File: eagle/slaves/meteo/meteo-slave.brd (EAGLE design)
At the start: 49.5 x 49.5 mm, 37 parts, among them CON1 SPI, IC1 MCP1703CB, J2 RJ12RIGHTANGLE-I2C, J3 RJ12RIGHTANGLE-I2C, U1 ATMEGA328P_TQFP, X1 8MHz, X2 1503_09, X3 1503_09

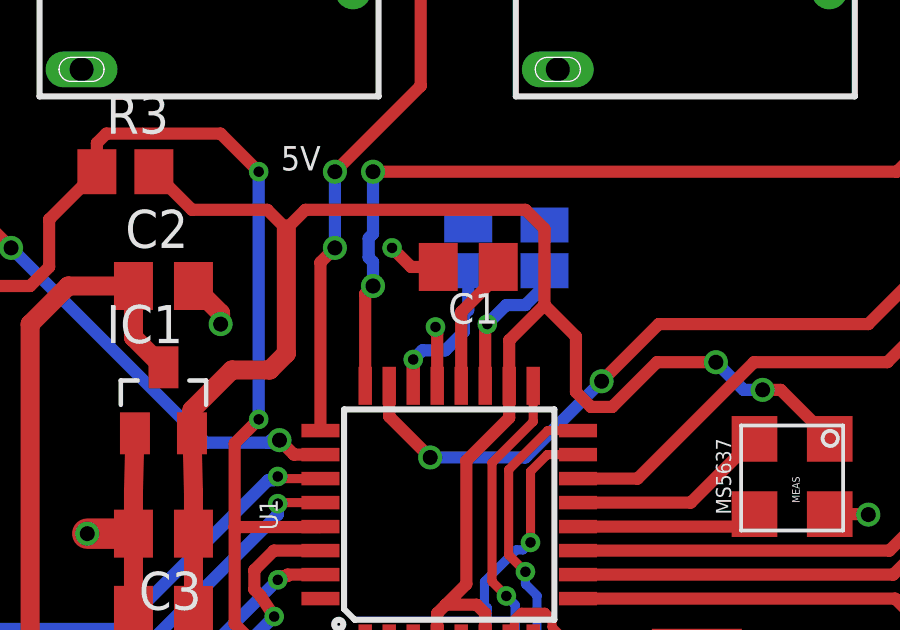
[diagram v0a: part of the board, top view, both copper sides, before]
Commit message: remove meteo capacitor for AREF
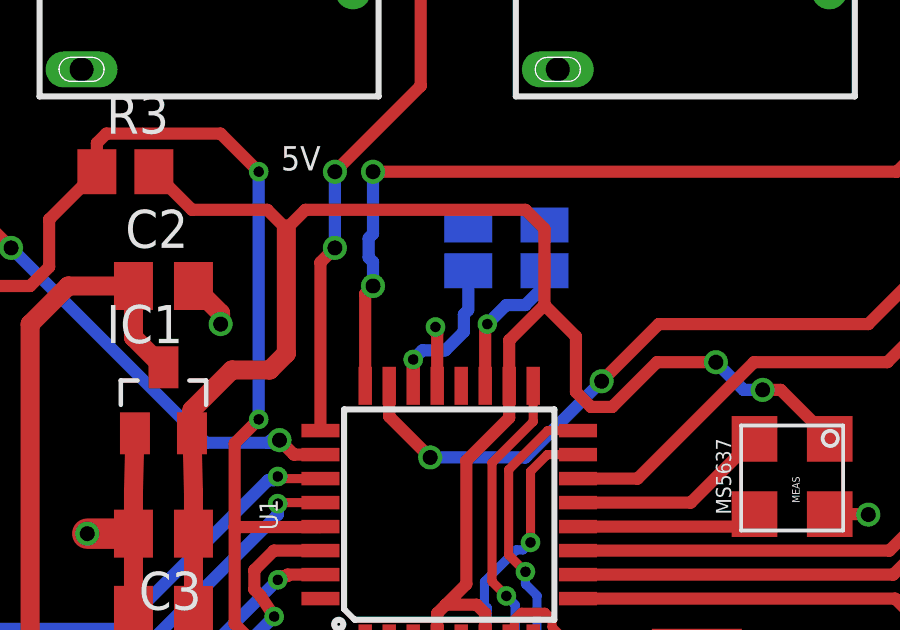
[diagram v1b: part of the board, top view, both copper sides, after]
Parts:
- removed C1: 100nF, rcl:C0805K
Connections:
- removed net AREF: C1.1, U1.20
- net GND: no longer C1.2
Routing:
- net AREF: track 4.47 -> 0.00 mm
- net GND: track 34.3 -> 32.5 mm, vias 13 -> 12
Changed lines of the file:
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@@
 <attribute name="VALUE" x="26.019" y="6.70695" size="1.016" layer="27" rot="R180"/>
-</element>
-<element name="C1" library="rcl" library_urn="urn:adsk.eagle:library:334" package="C0805K" package3d_urn="urn:adsk.eagle:package:23681/2" value="100nF" x="29.21" y="28.575" smashed="yes" rot="R180">
-<attribute name="ELECROW" value="C49678" x="29.21" y="28.575" size="1.778" layer="27" rot="R180" display="off"/>
-<attribute name="LCSC" value="C49678" x="29.21" y="28.575" size="1.778" layer="27" rot="R180" display="off"/>
-<attribute name="MPN" value="80-C1206C104K5R" x="29.21" y="28.575" size="1.778" layer="27" rot="R180" display="off"/>
-<attribute name="NAME" x="30.21" y="27.7" size="1.016" layer="25" rot="R180"/>
-<attribute name="VALUE" x="31.06725" y="30.8179" size="1.016" layer="27" rot="R180"/>
 </element>
 <element name="C5" library="rcl" library_urn="urn:adsk.eagle:library:334" package="C0805K" package3d_urn="urn:adsk.eagle:package:23681/2" value="100nF" x="27.305" y="12.7" smashed="yes" rot="R180">
@@
 <contactref element="C8" pad="1"/>
 <contactref element="C7" pad="1"/>
-<contactref element="C1" pad="2"/>
 <wire x1="40.005" y1="11.795" x2="40.005" y2="13.605" width="0.3048" layer="1"/>
 <wire x1="40.005" y1="11.795" x2="40.91" y2="11.795" width="0.3048" layer="1"/>
@@
 <wire x1="40.97168125" y1="14.5526" x2="41.16968125" y2="14.7506" width="0.3048" layer="1"/>
 <wire x1="41.16968125" y1="14.7506" x2="41.3824" y2="14.7506" width="0.3048" layer="1"/>
-<wire x1="28.21" y1="28.575" x2="27.305" y2="28.575" width="0.4064" layer="1"/>
-<wire x1="27.305" y1="28.575" x2="26.67" y2="29.21" width="0.4064" layer="1"/>
-<via x="26.67" y="29.21" extent="1-16" drill="0.35"/>
 <contactref element="U$1" pad="GND"/>
 <contactref element="U2" pad="GND"/>
@@
 <wire x1="2.286" y1="37.719" x2="2.54" y2="37.465" width="0.4064" layer="1"/>
 <via x="2.54" y="37.465" extent="1-16" drill="0.5"/>
+<wire x1="41.245" y1="38.36" x2="45.72" y2="40.005" width="0" layer="19" extent="1-1"/>
+<wire x1="31.75" y1="29.972" x2="41.245" y2="38.36" width="0" layer="19" extent="16-16"/>
+<wire x1="29.21" y1="29.972" x2="31.75" y2="29.972" width="0" layer="19" extent="16-16"/>
+<wire x1="28.1178" y1="26.57475" x2="29.21" y2="29.972" width="0" layer="19" extent="16-16"/>
+<wire x1="20.955" y1="26.67" x2="28.1178" y2="26.57475" width="0" layer="19" extent="1-1"/>
+<wire x1="18.1" y1="23.03" x2="20.955" y2="26.67" width="0" layer="19" extent="1-1"/>
+<wire x1="28.975" y1="16.0274" x2="28.175" y2="24.6126" width="0" layer="19" extent="1-1"/>
+<wire x1="27.375" y1="16.0274" x2="28.975" y2="16.0274" width="0" layer="19" extent="1-1"/>
+<wire x1="28.575" y1="8.1188" x2="25.4" y2="10.795" width="0" layer="19" extent="1-1"/>
+<wire x1="24.13" y1="4.445" x2="28.575" y2="8.1188" width="0" layer="19" extent="1-1"/>
+<wire x1="21.59" y1="4.445" x2="24.13" y2="4.445" width="0" layer="19" extent="1-1"/>
+<wire x1="38.1" y1="4.445" x2="30.48" y2="6.985" width="0" layer="19" extent="1-1"/>
+<wire x1="41.275" y1="11.43" x2="39.69" y2="4.445" width="0" layer="19" extent="1-1"/>
+<wire x1="45.72" y1="16.51" x2="41.3824" y2="14.7506" width="0" layer="19" extent="1-1"/>
+<wire x1="42.545" y1="20.32" x2="45.72" y2="16.51" width="0" layer="19" extent="1-1"/>
+<wire x1="25.37" y1="38.36" x2="29.21" y2="29.972" width="0" layer="19" extent="16-16"/>
+<wire x1="6.745" y1="16.51" x2="16.51" y2="19.685" width="0" layer="19" extent="1-1"/>
+<wire x1="6.745" y1="14.47" x2="6.745" y2="16.51" width="0" layer="19" extent="1-1"/>
+<wire x1="6.745" y1="30.345" x2="18.1" y2="23.03" width="0" layer="19" extent="1-1"/>
+<wire x1="6.745" y1="32.385" x2="6.745" y2="30.345" width="0" layer="19" extent="1-1"/>
+<wire x1="7.62" y1="37.465" x2="6.745" y2="32.385" width="0" layer="19" extent="1-1"/>
+<wire x1="2.54" y1="37.465" x2="7.62" y2="37.465" width="0" layer="19" extent="1-1"/>
 </signal>
 <signal name="SCK">
@@
 <signal name="N$16">
 </signal>
-<signal name="AREF">
-<contactref element="C1" pad="1"/>
-<wire x1="30.21" y1="28.305" x2="30.21" y2="28.575" width="0.4064" layer="1"/>
-<wire x1="28.975" y1="27.07" x2="30.21" y2="28.305" width="0.4064" layer="1"/>
-<contactref element="U1" pad="20"/>
-<wire x1="28.975" y1="24.6126" x2="28.975" y2="27.07" width="0.4064" layer="1"/>
-</signal>
 <signal name="TX">

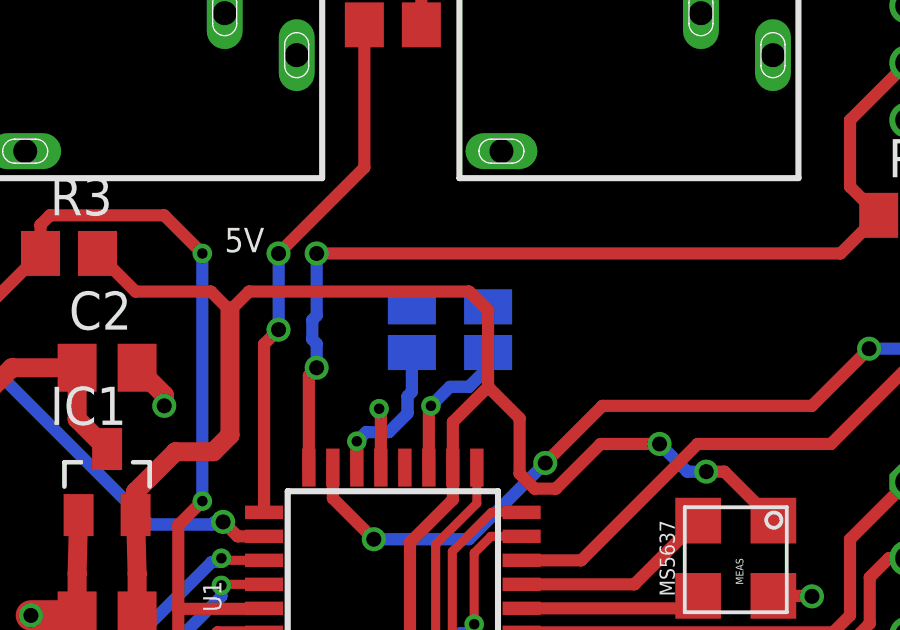
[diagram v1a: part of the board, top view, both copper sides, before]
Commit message: move address selector pad in meteo board
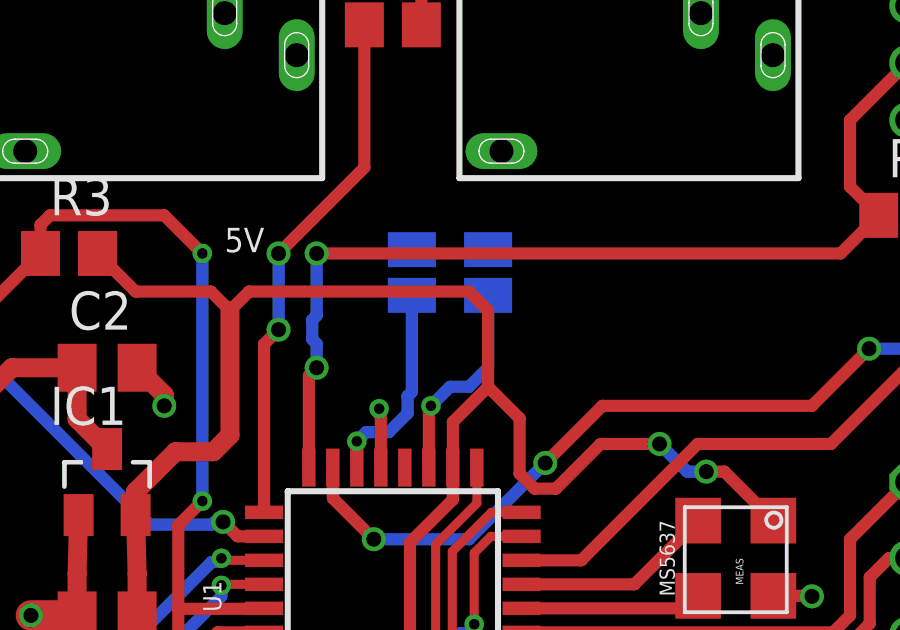
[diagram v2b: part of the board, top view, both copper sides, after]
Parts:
- moved SJ1 1.90 mm to (31.8, 31.1)
- moved SJ2 1.90 mm to (29.2, 31.1)
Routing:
- net A7: track 5.04 -> 6.95 mm
- net A6: track 5.03 -> 6.93 mm
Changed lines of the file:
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@@
 <layer number="199" name="Contour" color="7" fill="1" visible="no" active="yes"/>
 <layer number="200" name="200bmp" color="63" fill="10" visible="no" active="yes"/>
-<layer number="201" name="201bmp" color="63" fill="10" visible="yes" active="yes"/>
+<layer number="201" name="201bmp" color="63" fill="10" visible="no" active="yes"/>
 <layer number="202" name="202bmp" color="15" fill="1" visible="no" active="yes"/>
 <layer number="203" name="203bmp" color="2" fill="10" visible="no" active="yes"/>
@@
 <attribute name="VALUE" x="13.74645" y="14.65725" size="1.016" layer="27" rot="R270"/>
 </element>
-<element name="SJ1" library="jumper" library_urn="urn:adsk.eagle:library:252" package="SJ" package3d_urn="urn:adsk.eagle:package:15471/1" value="A0" x="31.75" y="29.21" smashed="yes" rot="MR90">
-<attribute name="NAME" x="32.893" y="27.559" size="1.27" layer="26" ratio="10" rot="MR90"/>
-<attribute name="VALUE" x="31.75" y="29.6101" size="0.02" layer="28" rot="MR90"/>
+<element name="SJ1" library="jumper" library_urn="urn:adsk.eagle:library:252" package="SJ" package3d_urn="urn:adsk.eagle:package:15471/1" value="A0" x="31.75" y="31.115" smashed="yes" rot="MR90">
+<attribute name="NAME" x="32.893" y="29.464" size="1.27" layer="26" ratio="10" rot="MR90"/>
+<attribute name="VALUE" x="31.75" y="31.5151" size="0.02" layer="28" rot="MR90"/>
 </element>
-<element name="SJ2" library="jumper" library_urn="urn:adsk.eagle:library:252" package="SJ" package3d_urn="urn:adsk.eagle:package:15471/1" value="A1" x="29.21" y="29.21" smashed="yes" rot="MR90">
-<attribute name="NAME" x="30.353" y="27.559" size="1.27" layer="26" ratio="10" rot="MR90"/>
-<attribute name="VALUE" x="29.21" y="29.6101" size="0.02" layer="28" rot="MR90"/>
+<element name="SJ2" library="jumper" library_urn="urn:adsk.eagle:library:252" package="SJ" package3d_urn="urn:adsk.eagle:package:15471/1" value="A1" x="29.21" y="31.115" smashed="yes" rot="MR90">
+<attribute name="NAME" x="30.353" y="29.464" size="1.27" layer="26" ratio="10" rot="MR90"/>
+<attribute name="VALUE" x="29.21" y="31.5151" size="0.02" layer="28" rot="MR90"/>
 </element>
 <element name="C7" library="rcl" library_urn="urn:adsk.eagle:library:334" package="C0805K" package3d_urn="urn:adsk.eagle:package:23681/2" value="18pF" x="40.005" y="10.795" smashed="yes" rot="R270">
@@
 <via x="2.54" y="37.465" extent="1-16" drill="0.5"/>
 <wire x1="41.245" y1="38.36" x2="45.72" y2="40.005" width="0" layer="19" extent="1-1"/>
-<wire x1="31.75" y1="29.972" x2="41.245" y2="38.36" width="0" layer="19" extent="16-16"/>
-<wire x1="29.21" y1="29.972" x2="31.75" y2="29.972" width="0" layer="19" extent="16-16"/>
-<wire x1="28.1178" y1="26.57475" x2="29.21" y2="29.972" width="0" layer="19" extent="16-16"/>
+<wire x1="31.75" y1="31.877" x2="41.245" y2="38.36" width="0" layer="19" extent="16-16"/>
+<wire x1="29.21" y1="31.877" x2="31.75" y2="31.877" width="0" layer="19" extent="16-16"/>
+<wire x1="28.1178" y1="26.57475" x2="29.21" y2="31.877" width="0" layer="19" extent="16-16"/>
 <wire x1="20.955" y1="26.67" x2="28.1178" y2="26.57475" width="0" layer="19" extent="1-1"/>
 <wire x1="18.1" y1="23.03" x2="20.955" y2="26.67" width="0" layer="19" extent="1-1"/>
@@
 <wire x1="45.72" y1="16.51" x2="41.3824" y2="14.7506" width="0" layer="19" extent="1-1"/>
 <wire x1="42.545" y1="20.32" x2="45.72" y2="16.51" width="0" layer="19" extent="1-1"/>
-<wire x1="25.37" y1="38.36" x2="29.21" y2="29.972" width="0" layer="19" extent="16-16"/>
+<wire x1="25.37" y1="38.36" x2="29.21" y2="31.877" width="0" layer="19" extent="16-16"/>
 <wire x1="6.745" y1="16.51" x2="16.51" y2="19.685" width="0" layer="19" extent="1-1"/>
 <wire x1="6.745" y1="14.47" x2="6.745" y2="16.51" width="0" layer="19" extent="1-1"/>
@@
 <wire x1="30.48" y1="27.305" x2="31.115" y2="27.305" width="0.4064" layer="16"/>
 <wire x1="31.115" y1="27.305" x2="31.75" y2="27.94" width="0.4064" layer="16"/>
-<wire x1="31.75" y1="27.94" x2="31.75" y2="28.448" width="0.4064" layer="16"/>
+<wire x1="31.75" y1="27.94" x2="31.75" y2="30.353" width="0.4064" layer="16"/>
 </signal>
 <signal name="A7">
@@
 <wire x1="28.4411375" y1="25.79415" x2="29.0644" y2="26.4174125" width="0.4064" layer="16"/>
 <wire x1="29.0644" y1="26.9933375" x2="29.21" y2="27.1389375" width="0.4064" layer="16"/>
-<wire x1="29.21" y1="27.1389375" x2="29.21" y2="28.448" width="0.4064" layer="16"/>
+<wire x1="29.21" y1="27.1389375" x2="29.21" y2="30.353" width="0.4064" layer="16"/>
 <wire x1="29.0644" y1="26.4174125" x2="29.0644" y2="26.9933375" width="0.4064" layer="16"/>
 </signal>
